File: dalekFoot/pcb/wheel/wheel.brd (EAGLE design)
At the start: 160 x 100 mm, 81 parts, among them IC1 LM1117MP-3.3, IC2 LM1117MP-3.3, IC3 LM1117MP-3.3, IC4 4051D, IC5 4051D, IC6 LM1117MP-3.3, K1 12X12-TACTILE, K2 12X12-TACTILE, K3 12X12-TACTILE, K4 12X12-TACTILE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

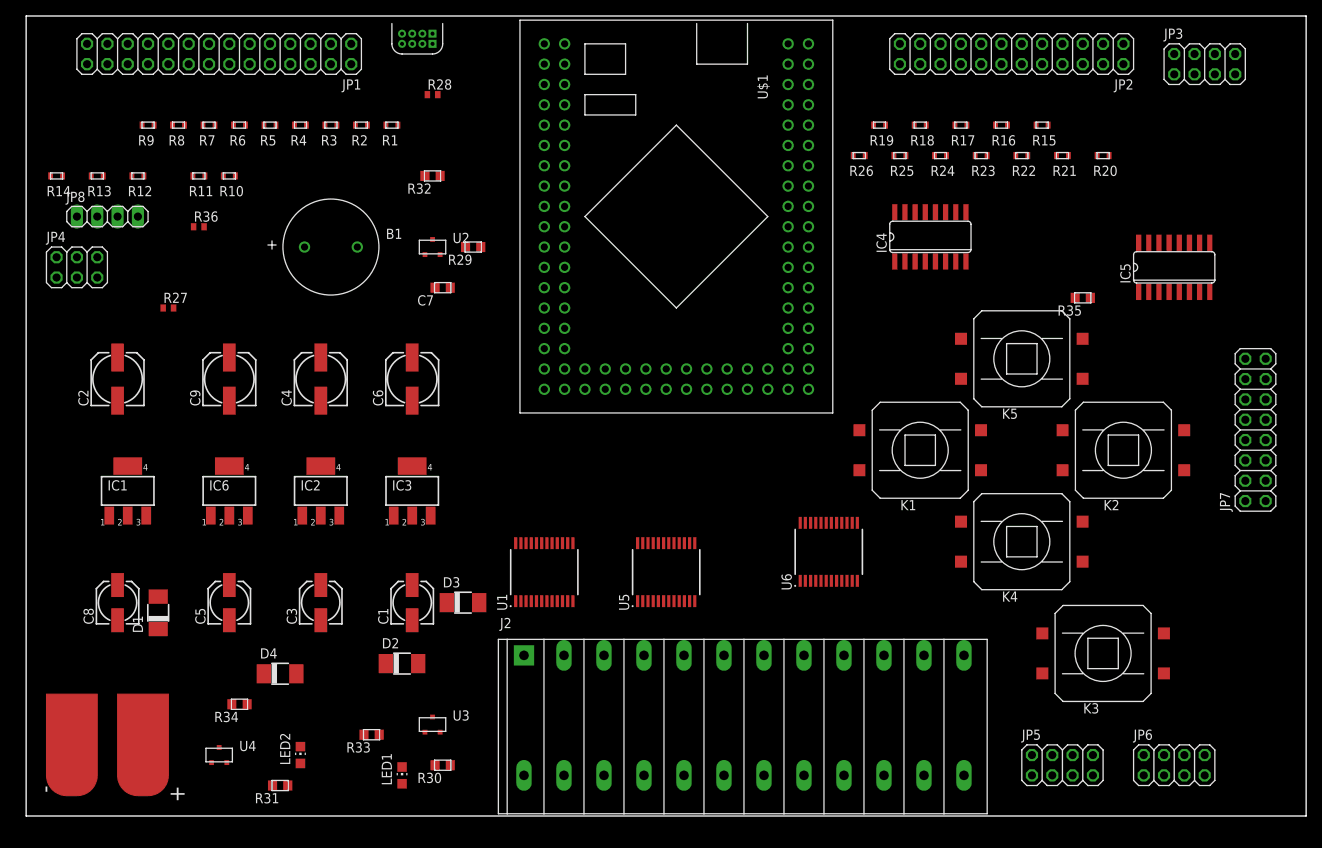
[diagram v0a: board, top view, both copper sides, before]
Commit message: place the parts in pcb, ready to route lines
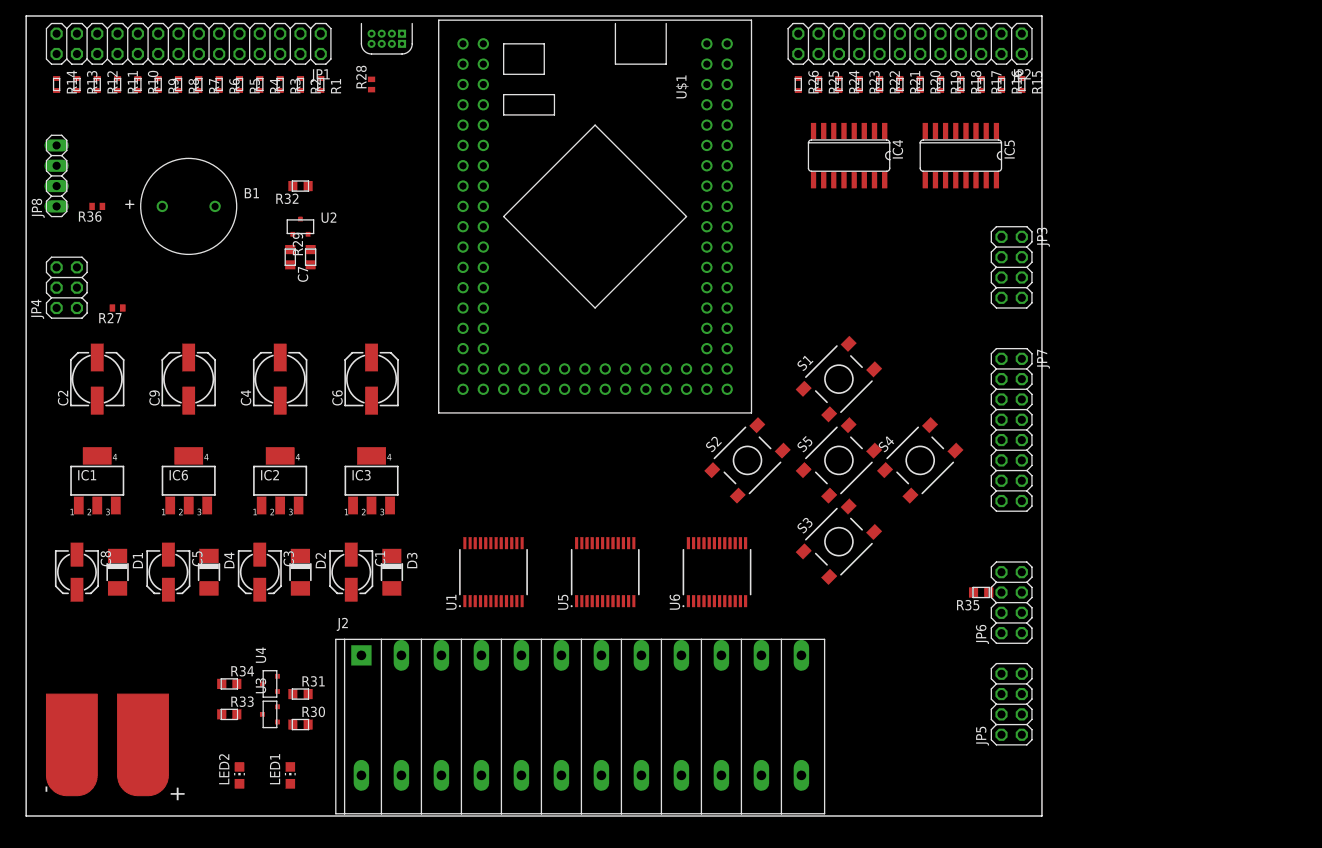
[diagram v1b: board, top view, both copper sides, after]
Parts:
- removed K1, K2, K3, K4, K5: 12X12-TACTILE, hqc:12X12-TACTILE
- added S1, S2, S3, S4, S5: DTSM-6, switch-tact:DTSM-6
- moved R35 39.0 mm to (119.4, 27.9)
- moved JP3 35.0 mm to (123.2, 68.6), turned to 270 degrees
- moved JP7 30.5 mm to (123.2, 48.3), turned to 270 degrees
- moved IC5 30.1 mm to (116.8, 82.5), turned to 180 degrees
- moved JP6 28.7 mm to (123.2, 26.7), turned to 90 degrees
- moved R20 24.5 mm to (111.8, 91.4), turned to 90 degrees
- moved R21 22.2 mm to (109.2, 91.4), turned to 90 degrees
- moved R29 20.4 mm to (35.6, 69.8), turned to 270 degrees
- moved U3 20.4 mm to (30.5, 12.7), turned to 90 degrees
- moved J2 20.3 mm to (41.9, 5.08)
- moved R22 19.9 mm to (106.7, 91.4), turned to 90 degrees
- moved C7 19.4 mm to (33.0, 69.8), turned to 90 degrees
- moved B1 18.5 mm to (20.3, 76.2)
- moved R30 18.5 mm to (34.3, 11.4), turned to 180 degrees
- moved R33 18.0 mm to (25.4, 12.7), turned to 180 degrees
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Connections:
- net BUT1: now also S1.1; no longer K1.P$A, K1.P$B
- net BUT2: now also S2.1; no longer K2.P$A, K2.P$B
- net BUT3: now also S3.1; no longer K3.P$A, K3.P$B
- net BUT4: now also S4.1; no longer K4.P$A, K4.P$B
- net BUT5: now also S5.1; no longer K5.P$A, K5.P$B
- net DGND: now also S1.3, S2.3, S3.3, S4.3, S5.3; no longer K1.P$C, K1.P$D, K2.P$C, K2.P$D, K3.P$C, K3.P$D, K4.P$C, K4.P$D, K5.P$C, K5.P$D
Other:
- board size 160 x 100 mm -> 127 x 100 mm

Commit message: update components positioning
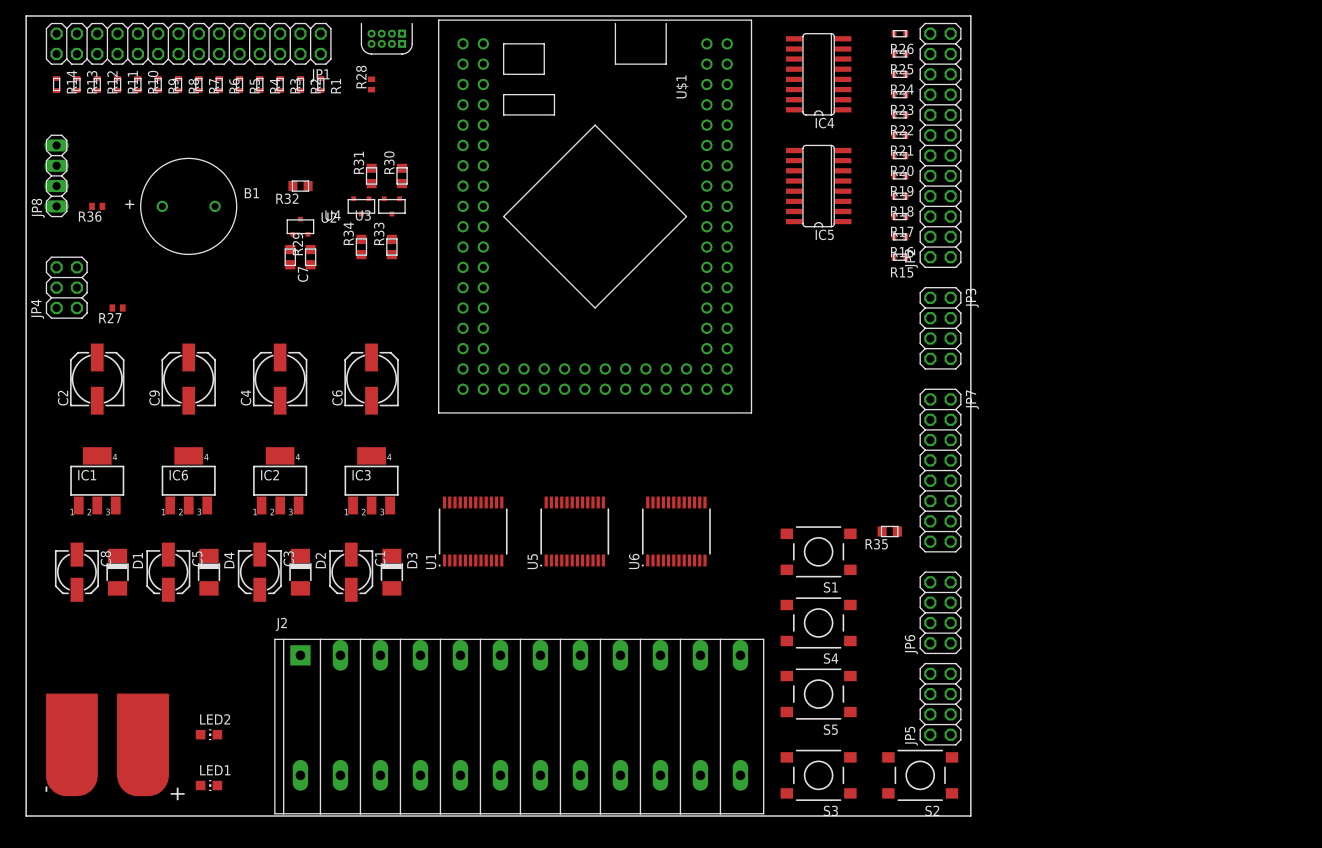
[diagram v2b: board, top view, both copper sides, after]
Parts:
- moved R30 69.7 mm to (47.0, 80.0), turned to 270 degrees
- moved R31 65.4 mm to (43.2, 80.0), turned to 270 degrees
- moved U3 65.3 mm to (45.7, 76.2), turned to 180 degrees
- moved R33 61.9 mm to (45.7, 71.1), turned to 270 degrees
- moved U4 60.8 mm to (41.9, 76.2), turned to 180 degrees
- moved R34 57.1 mm to (41.9, 71.1), turned to 270 degrees
- moved S2 44.9 mm to (111.8, 5.08), turned to 180 degrees
- moved S3 29.3 mm to (99.1, 5.08), turned to 180 degrees
- moved S5 29.3 mm to (99.1, 15.2), turned to 180 degrees
- moved R15 26.4 mm to (109.2, 69.8), turned to 0 degrees
- moved S4 24.0 mm to (99.1, 24.1), turned to 180 degrees
- moved R16 22.9 mm to (109.2, 72.4), turned to 0 degrees
- moved S1 21.7 mm to (99.1, 33.0), turned to 180 degrees
- moved R17 19.4 mm to (109.2, 74.9), turned to 0 degrees
- moved IC5 18.2 mm to (99.1, 78.7), turned to 90 degrees
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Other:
- board size 127 x 100 mm -> 118.1 x 100 mm

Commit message: 1. bugfix: fix net name typo 2. remove one unused phase power supply 3. make board more compact
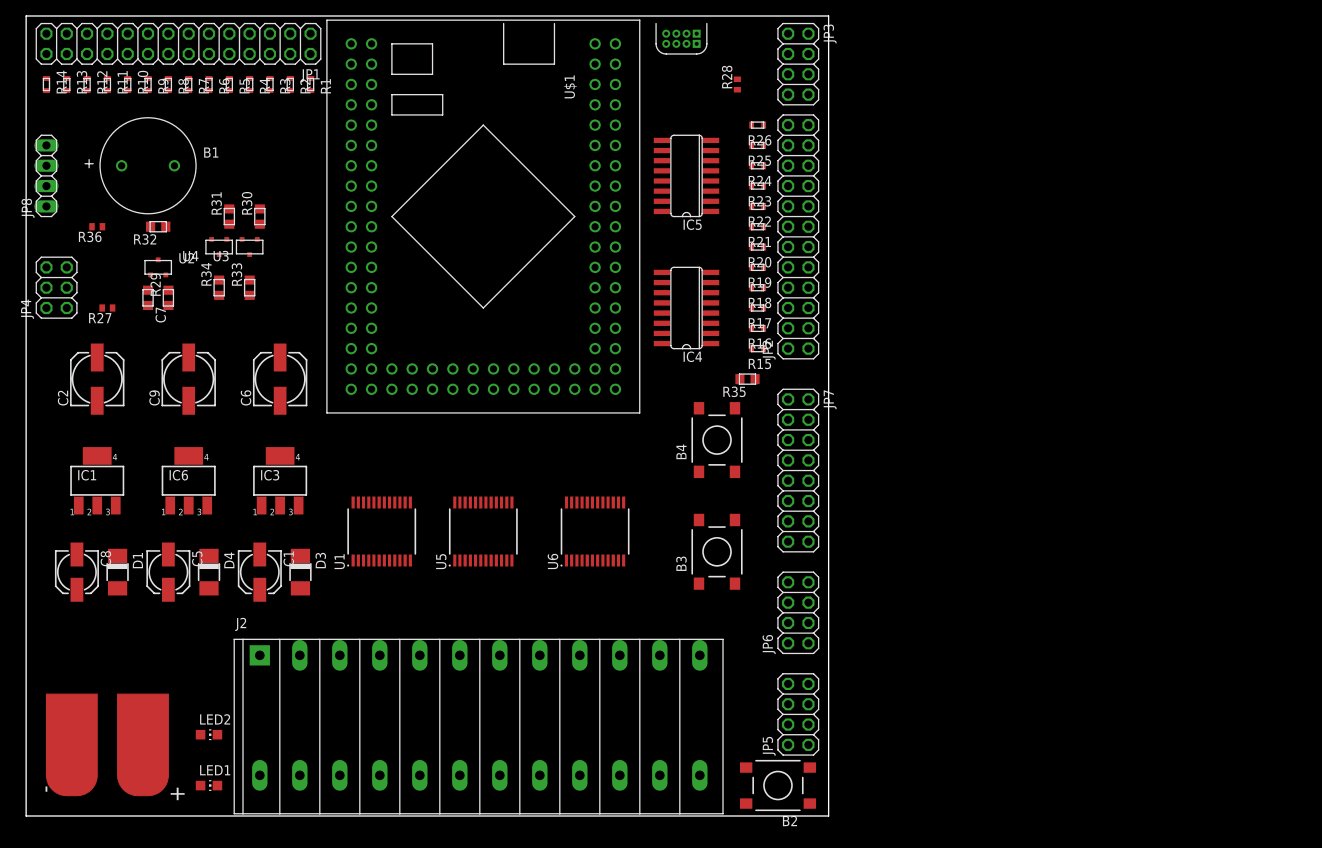
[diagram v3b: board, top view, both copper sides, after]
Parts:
- removed C3: 10uf, rcl:153CLV-0505
- removed C4: 100uf, rcl:153CLV-0605
- removed D2: (no value), diode:DO-214AC
- removed IC2: LM1117MP-3.3, lm1117:SOT223
- removed S1, S2, S3, S4, S5: DTSM-6, switch-tact:DTSM-6
- added B2, B3, B4: (no value), switch-tact:DTSM-6
- moved R28 45.7 mm to (88.9, 91.4)
- moved JP3 37.5 mm to (96.5, 94.0)
- moved J1 36.8 mm to (81.3, 99.1)
- moved IC4 33.6 mm to (82.5, 63.5)
- moved R35 26.1 mm to (90.2, 54.6)
- moved R17 21.1 mm to (91.4, 63.5)
- moved R19 21.1 mm to (91.4, 68.6)
- moved R21 21.1 mm to (91.4, 73.7)
- moved R23 21.1 mm to (91.4, 78.7)
- moved R25 21.1 mm to (91.4, 83.8)
- moved R26 21.1 mm to (91.4, 86.4)
- moved R16 21.1 mm to (91.4, 61.0)
- moved JP2 21.1 mm to (96.5, 72.4)
- moved R15 21.1 mm to (91.4, 58.4)
- moved R18 21.1 mm to (91.4, 66.0)
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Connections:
- removed net IR24\: IC5.15
- removed net N$1: D2.C, IC2.3
- removed net VCC-ANALOG: C4.+, IC2.2, IC2.4
- net BAT+: no longer C3.+, D2.A
- net BUT1: now also B2.1, B2.2; no longer S1.1
- net BUT2: now also B3.1, B3.2; no longer S2.1
- net BUT3: now also B4.1, B4.2; no longer S3.1
- net BUT4: no longer S4.1
- net BUT5: no longer S5.1
- net DGND: now also B2.3, B2.4, B3.3, B3.4, B4.3, B4.4; no longer C3.-, C4.-, IC2.1, S1.3, S2.3, S3.3, S4.3, S5.3
- net IR24: now also IC5.15
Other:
- board size 118.1 x 100 mm -> 100.3 x 100 mm

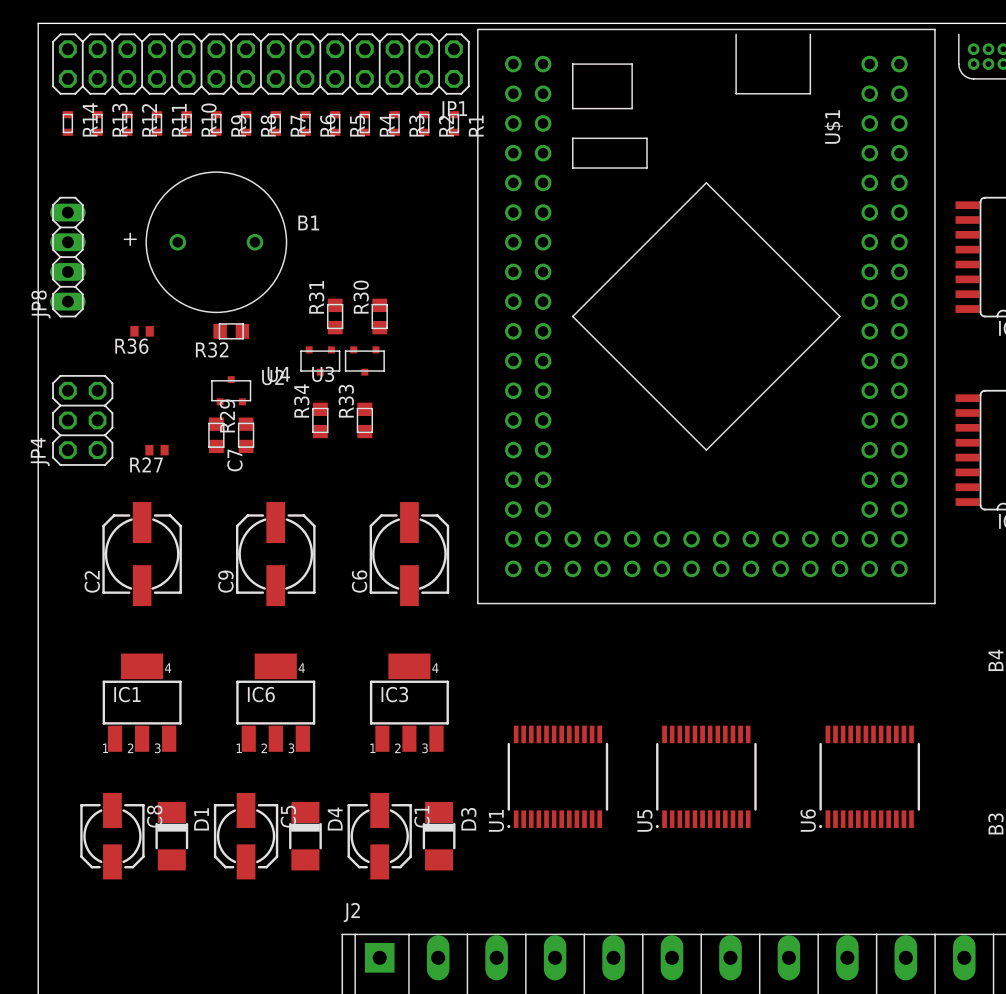
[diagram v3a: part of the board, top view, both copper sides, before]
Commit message: update pcb components layout
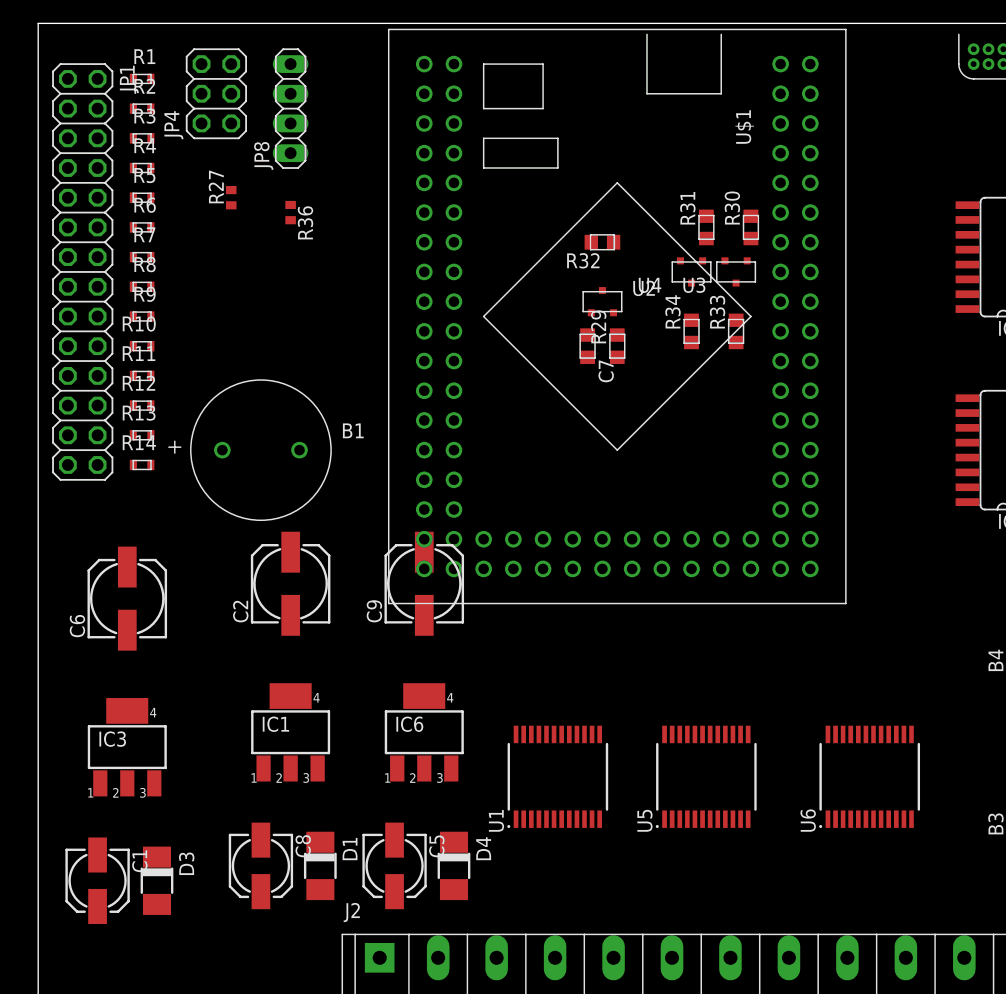
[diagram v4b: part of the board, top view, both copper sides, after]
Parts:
- moved R34 32.7 mm to (55.9, 73.7)
- moved U4 32.7 mm to (55.9, 78.7)
- moved C7 32.7 mm to (47.0, 72.4)
- moved R29 32.7 mm to (49.5, 72.4)
- moved R30 32.7 mm to (61.0, 82.5)
- moved R31 32.7 mm to (57.1, 82.5)
- moved R32 32.7 mm to (48.3, 81.3)
- moved R33 32.7 mm to (59.7, 73.7)
- moved U2 32.7 mm to (48.3, 76.2)
- moved U3 32.7 mm to (59.7, 78.7)
- moved JP4 30.2 mm to (15.2, 94.0)
- moved R14 29.9 mm to (8.89, 62.2), turned to 180 degrees
- moved R1 26.9 mm to (8.89, 95.2), turned to 180 degrees
- moved R13 26.9 mm to (8.89, 64.8), turned to 180 degrees
- moved C1 24.4 mm to (5.08, 26.7)
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
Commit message: try to add route hahhah
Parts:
- moved C9 9.25 mm to (24.1, 49.5)
- moved IC6 8.98 mm to (24.1, 38.1)
- moved C2 7.41 mm to (15.2, 48.3)
- moved IC1 6.48 mm to (15.2, 38.1)
- moved R30 5.08 mm to (55.9, 82.5)
- moved R31 5.08 mm to (52.1, 82.5)
- moved D4 4.02 mm to (31.8, 26.7)
- moved R34 4.02 mm to (52.1, 72.4)
- moved C5 4.02 mm to (26.7, 26.7)
- moved R33 4.02 mm to (55.9, 72.4)
- moved U4 3.81 mm to (52.1, 78.7)
- moved C8 2.84 mm to (16.5, 26.7)
- moved D1 2.84 mm to (21.6, 26.7)
- moved C7 2.54 mm to (44.5, 72.4)
- moved R29 2.54 mm to (47.0, 72.4)
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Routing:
- net DGND: track 0.00 -> 781.5 mm, vias 0 -> 15
- net VCC-DIGITAL: track 0.00 -> 369.2 mm, vias 0 -> 12
- net VCC-IR: track 0.00 -> 214.8 mm, vias 0 -> 2
- net BUT1: track 0.00 -> 170.6 mm, vias 0 -> 2
- net DIN1: track 0.00 -> 138.7 mm, vias 0 -> 1
- net DIN2: track 0.00 -> 130.4 mm, vias 0 -> 1
- net BUT2: track 0.00 -> 128.9 mm, vias 0 -> 2
- net USART_TX: track 0.00 -> 126.8 mm
- net BAT+: track 0.00 -> 116.8 mm
- net USART_RX: track 0.00 -> 114.5 mm
- net BUT3: track 0.00 -> 114.1 mm, vias 0 -> 2
- net N$20: track 0.00 -> 113.9 mm, vias 0 -> 4
- net DIN3: track 0.00 -> 95.3 mm, vias 0 -> 1
- net VCC-IRT: track 0.00 -> 93.5 mm, vias 0 -> 2
- net I2C2_SCL: track 0.00 -> 92.8 mm, vias 0 -> 3
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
